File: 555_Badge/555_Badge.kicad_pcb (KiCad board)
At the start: 2 copper layers, 53.8 x 85.6 mm, 15 parts, among them Q1 2N3904, U1 7555

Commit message: finished PCB design
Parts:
- moved BAT1 39.2 mm to (139.2, 121.9)
- moved C1 39.2 mm to (165.9, 120.7)
- moved Q1 39.2 mm to (165.9, 114.3)
- moved U1 39.2 mm to (157.0, 119.4)
- moved S1 39.2 mm to (154.4, 109.2)
- moved R4 38.4 mm to (178.6, 102.9)
- moved C2 38.4 mm to (174.8, 119.4)
- moved R1 38.4 mm to (159.5, 102.9)
- moved R2 38.4 mm to (163.3, 102.9)
- moved R3 38.4 mm to (174.8, 110.5)
- moved R5 38.4 mm to (170.9, 114.3)
- moved R6 38.4 mm to (167.1, 110.5)
- moved R7 38.4 mm to (170.9, 110.5)
- moved D1 24.2 mm to (160.3, 74.9), turned to 90 degrees
- moved D2 12.8 mm to (147.6, 74.9), turned to 90 degrees
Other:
- outline, holes or cut-outs redrawn

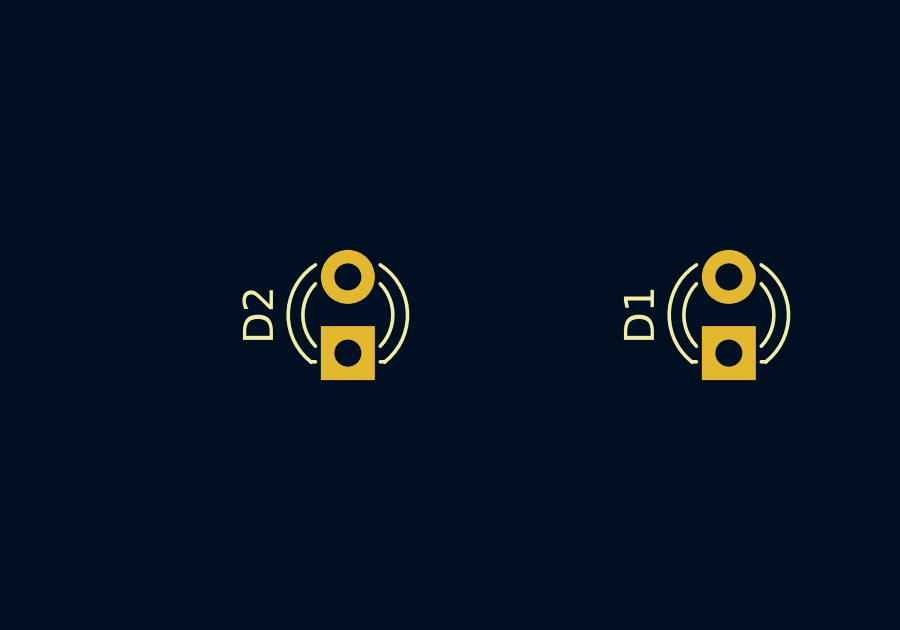
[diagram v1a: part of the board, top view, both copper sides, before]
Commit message: Adjusted wrong LED placement
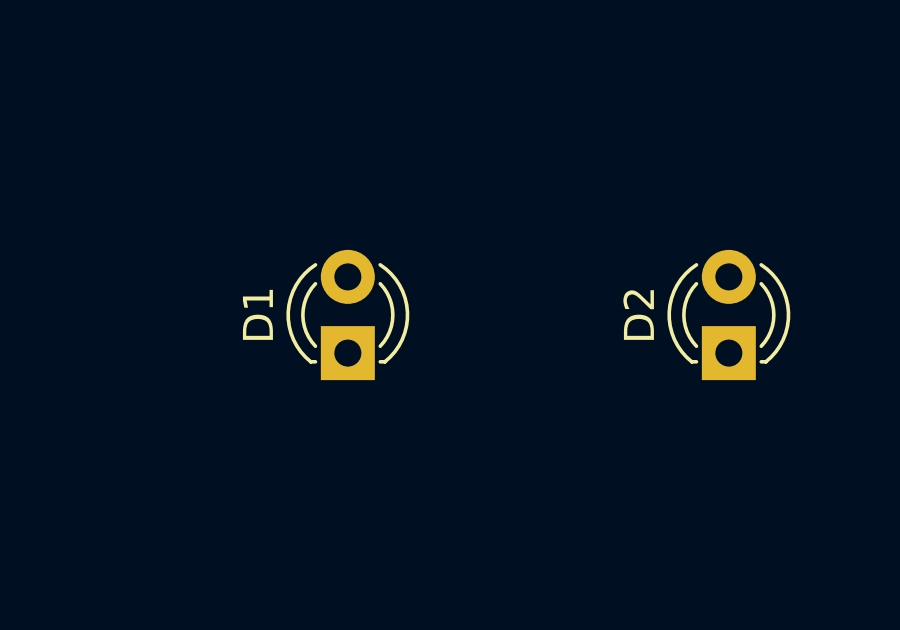
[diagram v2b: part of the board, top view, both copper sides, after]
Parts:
- moved D1 12.7 mm to (147.6, 74.9)
- moved D2 12.7 mm to (160.3, 74.9)

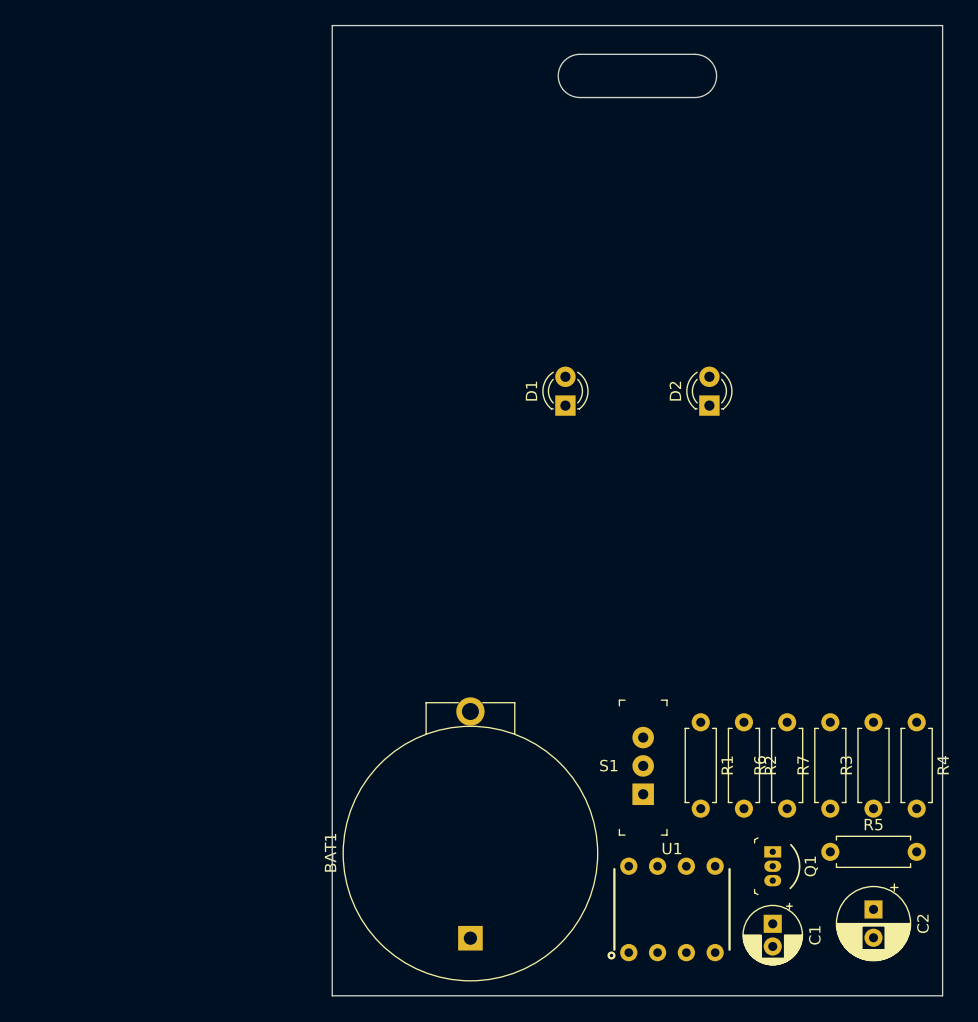
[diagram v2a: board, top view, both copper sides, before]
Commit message: Completed board layout
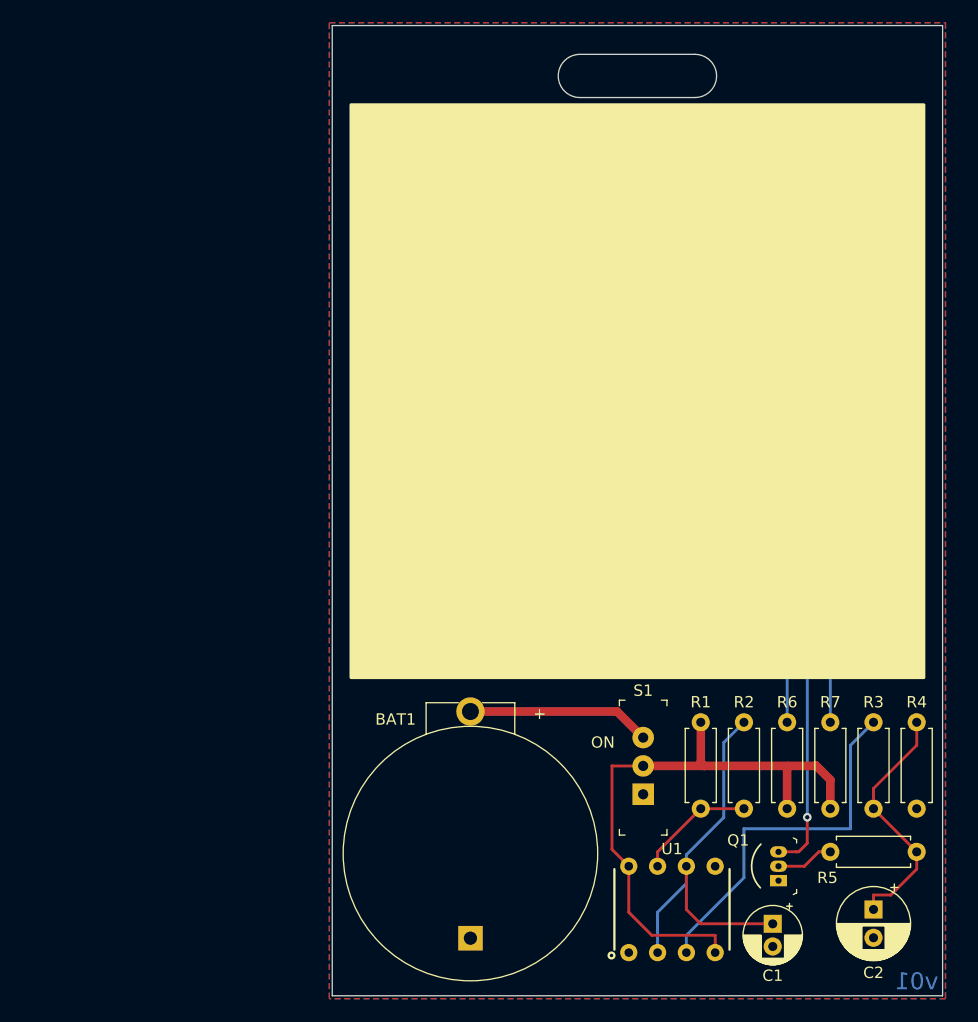
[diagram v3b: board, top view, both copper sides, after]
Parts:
- moved R2 7.62 mm to (163.3, 110.5), turned to 90 degrees
- moved Q1 2.59 mm to (166.4, 116.8), turned to 90 degrees
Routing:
- net Net-(D1-Pad1): track 0.00 -> 61.5 mm, vias 0 -> 1
- net Net-(D1-Pad2): track 0.00 -> 59.7 mm
- net VCC: track 0.00 -> 53.6 mm
- net Net-(D2-Pad2): track 0.00 -> 39.5 mm
- net Net-(C1-Pad1): track 0.00 -> 35.7 mm
- net Net-(R3-Pad2): track 0.00 -> 32.7 mm
- net Net-(C2-Pad1): track 0.00 -> 22.1 mm
- net Net-(BAT1-PadPos): track 0.00 -> 16.2 mm
- net Net-(R1-Pad2): track 0.00 -> 10.7 mm
- net Net-(Q1-Pad2): track 0.00 -> 5.10 mm
- added copper zone on B.Cu, net GND
- added copper zone on F.Cu, net GND
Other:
- board text added: "+"
- board text added: "555 Badge"
- board text added: "ON"
- board text added: "v01"
